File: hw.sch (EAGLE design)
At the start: 48 parts, among them IC1 MIC_I2S_SPH0645, IC2 CP2104, Q1 mmbt2222, Q2 mmbt2222, Q3 DMG3415U, SW2 KMR2, U1 MAX98357A, U2 AP2112-3.3, U3 MCP73831T-2ACI/OT, X2 JSTPH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

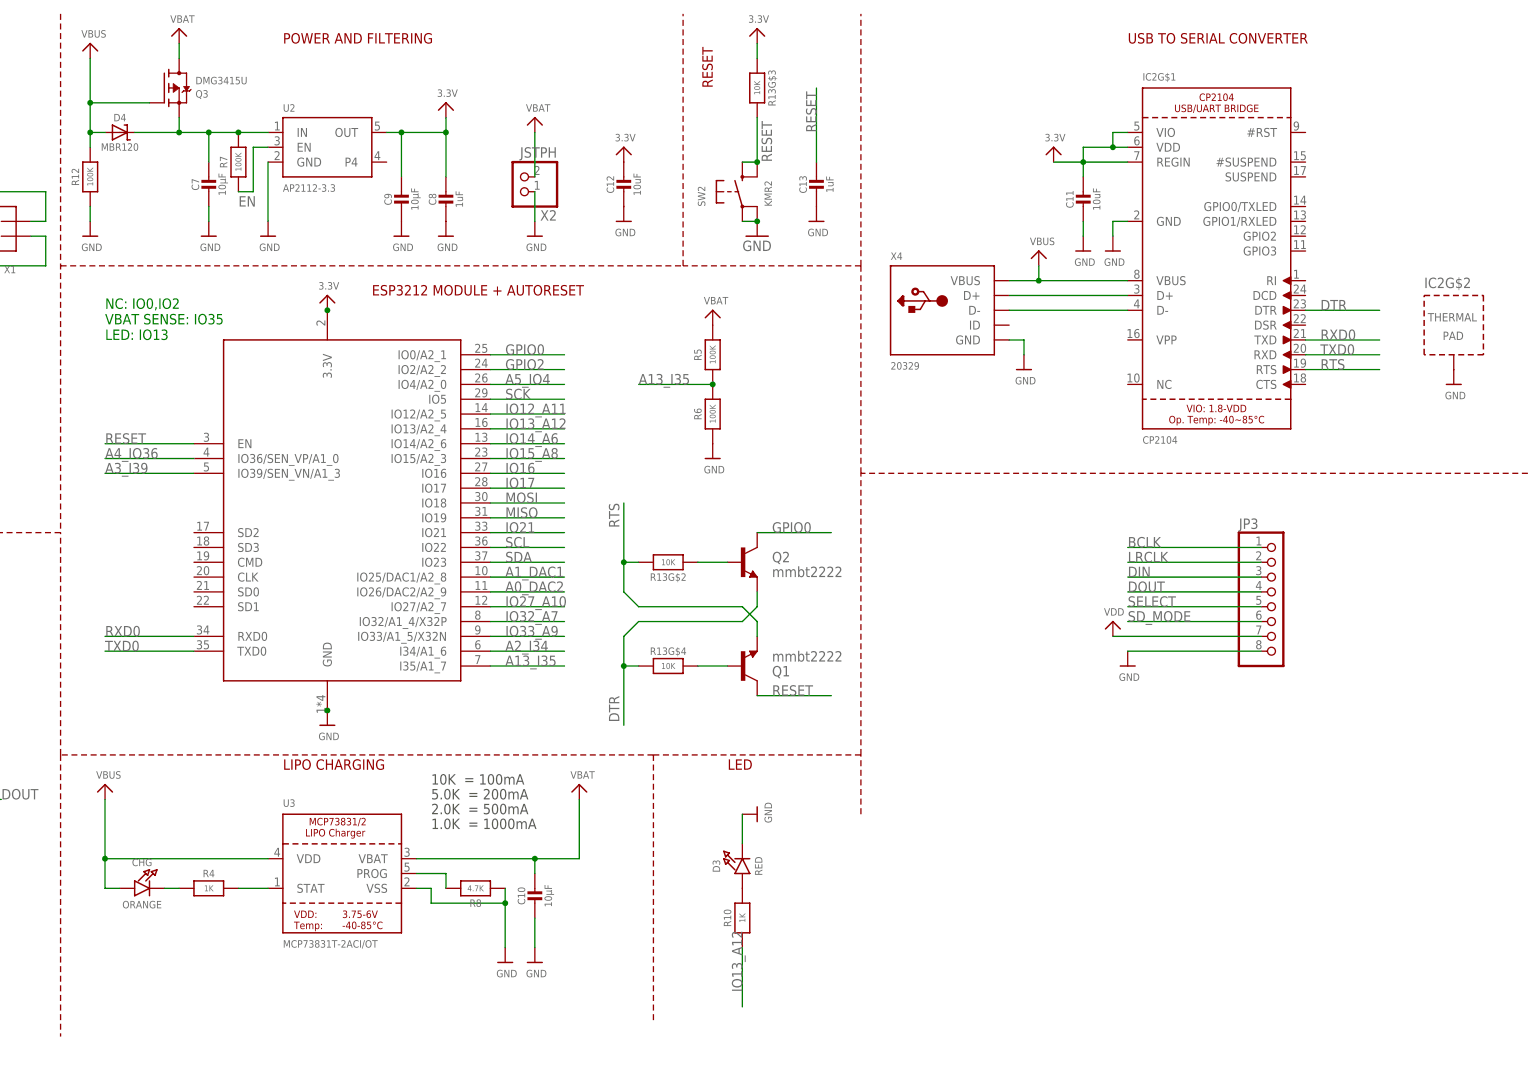
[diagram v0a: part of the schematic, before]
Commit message: using assembled esp32 devkitv1
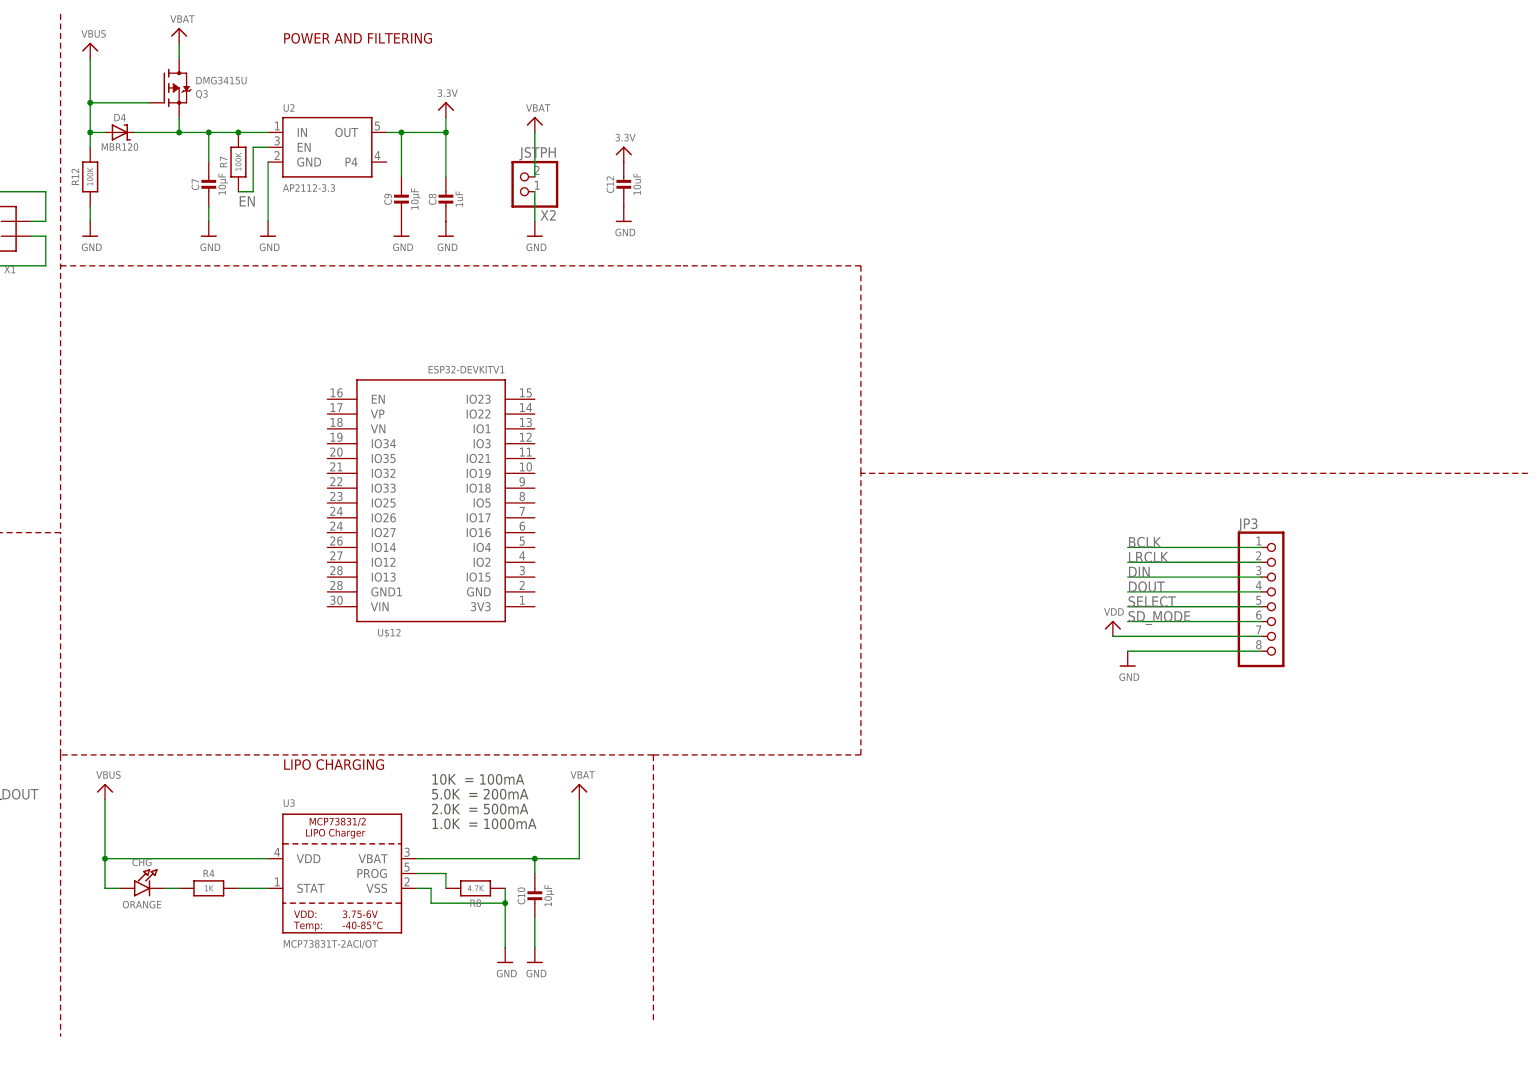
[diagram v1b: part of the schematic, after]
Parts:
- removed C11: 10uF, microbuilder:CAP_CERAMIC0805-NOOUTLINE
- removed C13: 1uF, microbuilder:CAP_CERAMIC0603_NO
- removed D3: RED, microbuilder:LED0805_NOOUTLINE
- removed IC2: CP2104, microbuilder:CP2104
- removed Q1, Q2: mmbt2222, SparkFun:TRANSISTOR_NPNSOT23-3
- removed R10: 1K, microbuilder:RESISTOR_0603_NOOUT
- removed R13: 10K, microbuilder:RESISTOR_4PACK
- removed R5, R6: 100K, microbuilder:RESISTOR_0603_NOOUT
- removed SW2: KMR2, microbuilder:SWITCH_TACT_SMT4.6X2.8
- removed X3: ESP32_WROOM32_SKINNY, microbuilder:ESP32_WROOM32_SKINNY
- removed X4: 20329, microbuilder:USB_MICRO_20329_V2
- added U$12: ESP32DEVKITV1, ESP32-DEVKITV1:ESP32DEVKITV1
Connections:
- removed net A0_DAC2: X3.IO26/DAC2/A2_9
- removed net A13_I35: R5.1, R6.2, X3.I35/A1_7
- removed net A1_DAC1: X3.IO25/DAC1/A2_8
- removed net A2_I34: X3.I34/A1_6
- removed net A3_I39: X3.IO39/SEN_VN/A1_3
- removed net A4_IO36: X3.IO36/SEN_VP/A1_0
- removed net A5_IO4: X3.IO4/A2_0
- removed net DTR: IC2G$1.DTR, Q2.E, R13G$4.1
- removed net GPIO0: Q2.C, X3.IO0/A2_1
- removed net GPIO2: X3.IO2/A2_2
- removed net IO12_A11: X3.IO12/A2_5
- removed net IO13_A12: R10.1, X3.IO13/A2_4
- removed net IO14_A6: X3.IO14/A2_6
- removed net IO15_A8: X3.IO15/A2_3
- removed net IO16: X3.IO16
- removed net IO17: X3.IO17
- removed net IO21: X3.IO21
- removed net IO27_A10: X3.IO27/A2_7
- removed net IO32_A7: X3.IO32/A1_4/X32P
- removed net IO33_A9: X3.IO33/A1_5/X32N
- removed net MISO: X3.IO19
- removed net MOSI: X3.IO18
- removed net N$10: D3.A, R10.2
- removed net N$12: Q1.B, R13G$4.2
- removed net N$13: Q2.B, R13G$2.1
- removed net N$7: IC2G$1.D+, X4.D+
- removed net N$8: IC2G$1.D-, X4.D-
- removed net RESET: C13.1, Q1.C, R13G$3.2, SW2.S, SW2.S1, X3.EN
- removed net RTS: IC2G$1.RTS, Q1.E, R13G$2.2
- removed net RXD0: IC2G$1.TXD, X3.RXD0
- removed net SCK: X3.IO5
- removed net TXD0: IC2G$1.RXD, X3.TXD0
- net 3.3V: no longer C11.1, IC2G$1.REGIN, IC2G$1.VDD, IC2G$1.VIO, R13G$3.1, X3.3.3V
- net GND: no longer C11.2, C13.2, D3.C, IC2G$1.GND, IC2G$2.TP, R6.1, SW2.P, SW2.P1, X3.GND, X4.GND
- net SCL: no longer X3.IO22
- net SDA: no longer X3.IO23
- net VBAT: no longer R5.2
- net VBUS: no longer IC2G$1.VBUS, X4.VBUS
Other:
- note removed: "ESP3212 MODULE + AUTORESET"
- note removed: "LED"
- note removed: "NC: IO0,IO2 VBAT SENSE: IO35 LED: IO13"
- note removed: "RESET"
- note removed: "USB TO SERIAL CONVERTER"

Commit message: routing
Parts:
- removed JP3: (no value), adafruit:PINHD-1X8BIG
- added JP1: (no value), microbuilder:HEADER-1X7THICKER
- added JP2: (no value), microbuilder:HEADER-1X6ROUND
- R11, R9: value (none) -> 10k
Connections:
- new net BTN1: S2.2, U$12.IO23
- new net BTN2: S1.2, U$12.IO22
- new net DATA: JP2.4, U$12.IO26
- new net N$12: U$12.IO27
- net BCLK: now also JP1.6, JP2.3, U$12.IO32; no longer JP3.1
- net DIN: now also JP1.5, U$12.IO25; no longer JP3.3
- net DOUT: no longer JP3.4
- net GAIN: now also JP1.4
- net GND: now also JP1.2, JP2.2, S1.1, S2.1; no longer JP3.8
- net LRCLK: now also JP1.7, JP2.5, U$12.IO33; no longer JP3.2
- net SD_MODE: now also JP1.3; no longer JP3.6
- net SELECT: now also JP2.6, U$12.IO14; no longer JP3.5
- net VDD: now also JP1.1, JP2.1; no longer JP3.7

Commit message: more routing
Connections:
- removed net DATA: JP2.4, U$12.IO26
- net DOUT: now also JP2.4, U$12.IO26
- net SCL: now also U$12.IO19
- net SDA: now also U$12.IO21
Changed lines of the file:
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@@
 <wire x1="152.4" y1="50.8" x2="157.48" y2="50.8" width="0.1524" layer="91"/>
+</segment>
+<segment>
+<label x="157.48" y="50.8" size="1.778" layer="95"/>
+</segment>
+<segment>
+<pinref part="U$12" gate="G$1" pin="IO26"/>
+<wire x1="213.36" y1="99.06" x2="208.28" y2="99.06" width="0.1524" layer="91"/>
+<label x="208.28" y="99.06" size="1.778" layer="95"/>
+<label x="208.28" y="96.52" size="1.778" layer="95"/>
+</segment>
+<segment>
+<pinref part="JP2" gate="A" pin="4"/>
+<wire x1="373.38" y1="50.8" x2="337.82" y2="50.8" width="0.1524" layer="91"/>
+<label x="337.82" y="50.8" size="1.778" layer="95"/>
 </segment>
 </net>
@@
 <junction x="-25.4" y="27.94"/>
 </segment>
+<segment>
+<pinref part="U$12" gate="G$1" pin="IO21"/>
+<wire x1="248.92" y1="109.22" x2="256.54" y2="109.22" width="0.1524" layer="91"/>
+<label x="256.54" y="109.22" size="1.778" layer="95"/>
+<label x="256.54" y="109.22" size="1.778" layer="95"/>
+<label x="256.54" y="109.22" size="1.778" layer="95"/>
+</segment>
 </net>
 <net name="SCL" class="0">
@@
 <wire x1="-20.32" y1="33.02" x2="-10.16" y2="33.02" width="0.1524" layer="91"/>
 <junction x="-10.16" y="33.02"/>
+</segment>
+<segment>
+<pinref part="U$12" gate="G$1" pin="IO19"/>
+<wire x1="248.92" y1="106.68" x2="256.54" y2="106.68" width="0.1524" layer="91"/>
+<label x="256.54" y="106.68" size="1.778" layer="95"/>
 </segment>
 </net>
@@
 </segment>
 </net>
-<net name="DATA" class="0">
-<segment>
-<pinref part="JP2" gate="A" pin="4"/>
-<wire x1="373.38" y1="50.8" x2="337.82" y2="50.8" width="0.1524" layer="91"/>
-<label x="337.82" y="50.8" size="1.778" layer="95"/>
-</segment>
-<segment>
-<pinref part="U$12" gate="G$1" pin="IO26"/>
-<wire x1="213.36" y1="99.06" x2="208.28" y2="99.06" width="0.1524" layer="91"/>
-<label x="208.28" y="99.06" size="1.778" layer="95"/>
-<label x="208.28" y="96.52" size="1.778" layer="95"/>
-</segment>
-<segment>
-<label x="157.48" y="50.8" size="1.778" layer="95"/>
-</segment>
-</net>

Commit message: rerouting :|
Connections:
- removed net N$12: U$12.IO27
- removed net VCC: R11.2, R9.2, U$1.VCC
- removed net WS: IC1.WS
- net 3.3V: now also C1.1, C2.1, C3.1, C6.1, IC1.VDD, JP1.1, JP2.1, R1.2, U$12.3V3, U1.VDD
- net BCLK: now also U$12.IO17; no longer U$12.IO32
- net BTN1: now also U$12.IO12; no longer U$12.IO23
- net BTN2: now also U$12.IO13; no longer U$12.IO22
- net DIN: now also U$12.IO18; no longer U$12.IO25
- net DOUT: now also U$12.IO4; no longer U$12.IO26
- net GAIN: no longer JP1.4
- net GND: now also U$12.GND
- net LRCLK: now also IC1.WS, U$12.IO16; no longer U$12.IO33
- net SCL: now also U$12.IO21; no longer U$12.IO19
- net SDA: now also U$12.IO19; no longer U$12.IO21
- net SD_MODE: no longer JP1.3
- net SELECT: no longer JP2.6, U$12.IO14
- net VDD: now also R11.2, R9.2, U$1.VCC, U$12.VIN; no longer C1.1, C2.1, C3.1, C6.1, IC1.VDD, JP1.1, JP2.1, R1.2, U1.VDD

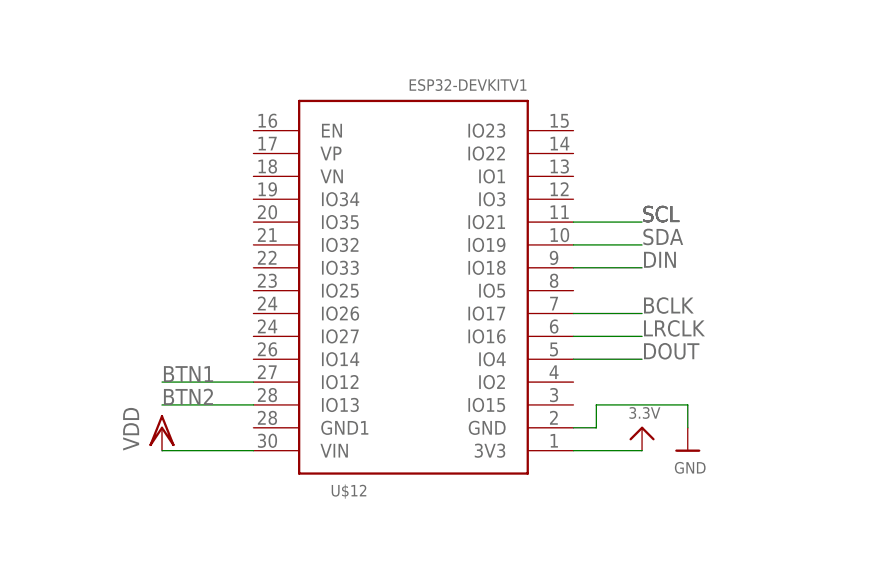
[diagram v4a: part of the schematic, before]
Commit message: it works out!
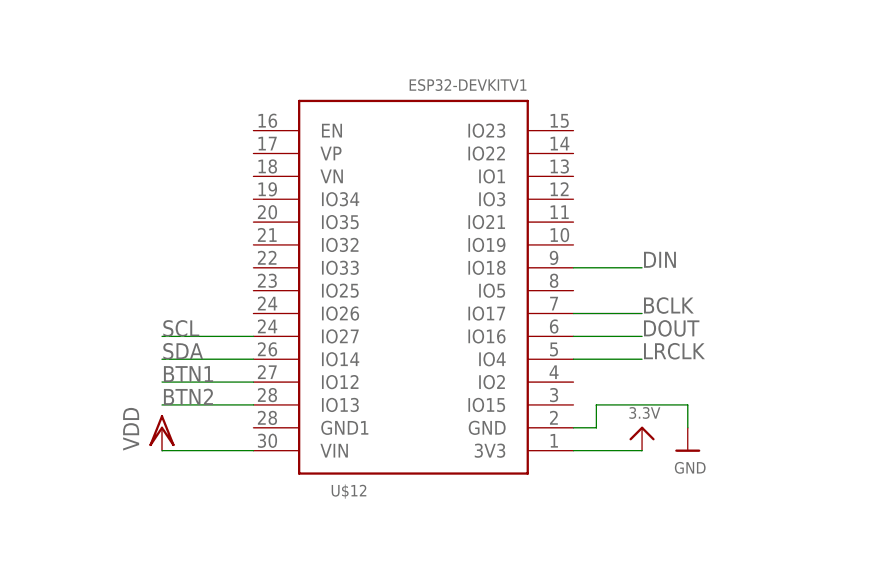
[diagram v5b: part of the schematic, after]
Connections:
- net DOUT: now also U$12.IO16; no longer U$12.IO4
- net LRCLK: now also U$12.IO4; no longer U$12.IO16
- net SCL: now also U$12.IO27; no longer U$12.IO21
- net SDA: now also U$12.IO14; no longer U$12.IO19
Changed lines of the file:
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@@
+</segment>
+<segment>
+<pinref part="U$12" gate="G$1" pin="IO4"/>
+<wire x1="248.92" y1="93.98" x2="256.54" y2="93.98" width="0.1524" layer="91"/>
+<label x="256.54" y="93.98" size="1.778" layer="95"/>
+</segment>
+</net>
+<net name="DIN" class="0">
+<segment>
+<pinref part="U1" gate="G$1" pin="DIN"/>
+<wire x1="86.36" y1="144.78" x2="71.12" y2="144.78" width="0.1524" layer="91"/>
+<label x="71.12" y="144.78" size="1.778" layer="95"/>
+</segment>
+<segment>
+<wire x1="414.02" y1="50.8" x2="391.16" y2="50.8" width="0.1524" layer="91"/>
+<pinref part="JP1" gate="A" pin="5"/>
+<label x="391.16" y="50.8" size="1.778" layer="95"/>
+</segment>
+<segment>
+<pinref part="U$12" gate="G$1" pin="IO18"/>
+<wire x1="248.92" y1="104.14" x2="256.54" y2="104.14" width="0.1524" layer="91"/>
+<label x="256.54" y="104.14" size="1.778" layer="95"/>
+</segment>
+</net>
+<net name="GAIN" class="0">
+<segment>
+<pinref part="U1" gate="G$1" pin="GAIN"/>
+<wire x1="116.84" y1="137.16" x2="124.46" y2="137.16" width="0.1524" layer="91"/>
+<label x="116.84" y="137.16" size="1.778" layer="95"/>
+</segment>
+</net>
+<net name="DOUT" class="0">
+<segment>
+<pinref part="R2" gate="G$1" pin="2"/>
+<wire x1="152.4" y1="50.8" x2="157.48" y2="50.8" width="0.1524" layer="91"/>
+</segment>
+<segment>
+<label x="157.48" y="50.8" size="1.778" layer="95"/>
+</segment>
+<segment>
+<pinref part="JP2" gate="A" pin="4"/>
+<wire x1="373.38" y1="50.8" x2="337.82" y2="50.8" width="0.1524" layer="91"/>
+<label x="337.82" y="50.8" size="1.778" layer="95"/>
 </segment>
 <segment>
@@
 <wire x1="248.92" y1="96.52" x2="256.54" y2="96.52" width="0.1524" layer="91"/>
 <label x="256.54" y="96.52" size="1.778" layer="95"/>
-</segment>
-</net>
-<net name="DIN" class="0">
-<segment>
-<pinref part="U1" gate="G$1" pin="DIN"/>
-<wire x1="86.36" y1="144.78" x2="71.12" y2="144.78" width="0.1524" layer="91"/>
-<label x="71.12" y="144.78" size="1.778" layer="95"/>
-</segment>
-<segment>
-<wire x1="414.02" y1="50.8" x2="391.16" y2="50.8" width="0.1524" layer="91"/>
-<pinref part="JP1" gate="A" pin="5"/>
-<label x="391.16" y="50.8" size="1.778" layer="95"/>
-</segment>
-<segment>
-<pinref part="U$12" gate="G$1" pin="IO18"/>
-<wire x1="248.92" y1="104.14" x2="256.54" y2="104.14" width="0.1524" layer="91"/>
-<label x="256.54" y="104.14" size="1.778" layer="95"/>
-</segment>
-</net>
-<net name="GAIN" class="0">
-<segment>
-<pinref part="U1" gate="G$1" pin="GAIN"/>
-<wire x1="116.84" y1="137.16" x2="124.46" y2="137.16" width="0.1524" layer="91"/>
-<label x="116.84" y="137.16" size="1.778" layer="95"/>
-</segment>
-</net>
-<net name="DOUT" class="0">
-<segment>
-<pinref part="R2" gate="G$1" pin="2"/>
-<wire x1="152.4" y1="50.8" x2="157.48" y2="50.8" width="0.1524" layer="91"/>
-</segment>
-<segment>
-<label x="157.48" y="50.8" size="1.778" layer="95"/>
-</segment>
-<segment>
-<pinref part="JP2" gate="A" pin="4"/>
-<wire x1="373.38" y1="50.8" x2="337.82" y2="50.8" width="0.1524" layer="91"/>
-<label x="337.82" y="50.8" size="1.778" layer="95"/>
-</segment>
-<segment>
-<pinref part="U$12" gate="G$1" pin="IO4"/>
-<wire x1="248.92" y1="93.98" x2="256.54" y2="93.98" width="0.1524" layer="91"/>
-<label x="256.54" y="93.98" size="1.778" layer="95"/>
 </segment>
 </net>
@@
 </segment>
 <segment>
-<pinref part="U$12" gate="G$1" pin="IO19"/>
-<wire x1="248.92" y1="106.68" x2="256.54" y2="106.68" width="0.1524" layer="91"/>
-<label x="256.54" y="106.68" size="1.778" layer="95"/>
+<pinref part="U$12" gate="G$1" pin="IO14"/>
+<wire x1="213.36" y1="93.98" x2="203.2" y2="93.98" width="0.1524" layer="91"/>
+<label x="203.2" y="93.98" size="1.778" layer="95"/>
 </segment>
 </net>
@@
 </segment>
 <segment>
-<pinref part="U$12" gate="G$1" pin="IO21"/>
-<wire x1="248.92" y1="109.22" x2="256.54" y2="109.22" width="0.1524" layer="91"/>
-<label x="256.54" y="109.22" size="1.778" layer="95"/>
-<label x="256.54" y="109.22" size="1.778" layer="95"/>
-<label x="256.54" y="109.22" size="1.778" layer="95"/>
-</segment>
-</net>
+<pinref part="U$12" gate="G$1" pin="IO27"/>
+<wire x1="213.36" y1="96.52" x2="203.2" y2="96.52" width="0.1524" layer="91"/>
+<label x="203.2" y="96.52" size="1.778" layer="95"/>
+</segment>
+</net>

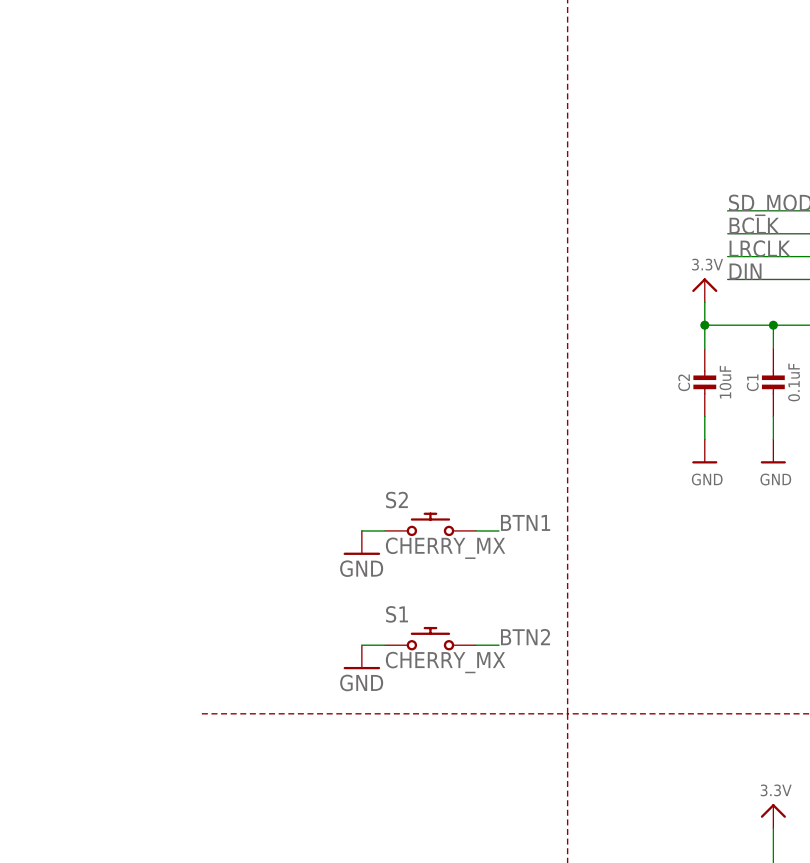
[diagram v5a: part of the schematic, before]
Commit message: changing cherrymx part to avoid large etch-off area
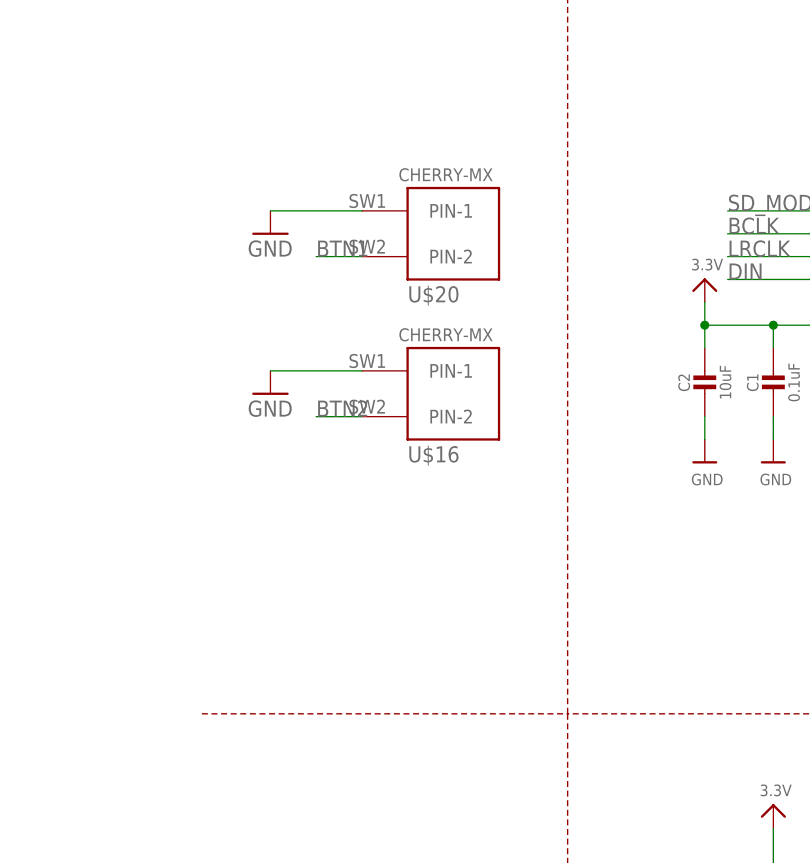
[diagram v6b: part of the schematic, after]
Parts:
- removed S1, S2: CHERRY_MX, cherry:CHERRY_MX
- added U$16, U$20: CHERRY-MX, cherrymx:CHERRY-MX
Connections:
- net BTN1: now also U$20.PIN-2; no longer S2.2
- net BTN2: now also U$16.PIN-2; no longer S1.2
- net GND: now also U$16.PIN-1, U$20.PIN-1; no longer S1.1, S2.1
